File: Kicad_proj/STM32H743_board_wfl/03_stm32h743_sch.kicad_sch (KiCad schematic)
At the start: 35 parts, among them J1 GPS, J2 ESC, J3 UART, J4 Tag_Connect_6pin, U3 STM32H743VITx, U4 W25Q512JVEIQ, Y1 TSX-3225_16.0000MF18X-AC0

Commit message: update stm32 quartz caps + prebom
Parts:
- C23, C24: value 27pF -> 10pF
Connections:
- net GND: now also Y1.2 (G), Y1.4 (G)
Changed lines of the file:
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@@
 	(wire
 		(pts
+			(xy 181.356 89.154) (xy 184.15 89.154)
+		)
+		(stroke
+			(width 0)
+			(type default)
+		)
+	)
+	(wire
+		(pts
 			(xy 231.394 42.164) (xy 228.854 42.164)
 		)
@@
 			)
 		)
-		(property "Value" "27pF"
+		(property "Value" "10pF"
 			(at 156.464 99.0599 0)
 			(show_name no)
@@
 			)
 		)
-		(property "Datasheet" "https://www.mouser.pl/pl/ProductDetail/KYOCERA-AVX/04023U270JAT2A?qs=%252BdQmOuGyFcGHQXol69SFgA%3D%3D"
+		(property "Datasheet" "https://www.tme.eu/pl/details/grm1555c1h100ga01d/kondensatory-mlcc-smd/murata/"
 			(at 160.528 97.79 0)
 			(hide yes)
@@
 	)
 	(symbol
+		(lib_id "power:GND")
+		(at 184.15 89.154 90)
+		(mirror x)
+		(unit 1)
+		(body_style 1)
+		(exclude_from_sim no)
+		(in_bom yes)
+		(on_board yes)
+		(in_pos_files yes)
+		(dnp no)
+		(fields_autoplaced yes)
+		(property "Reference" "#PWR068"
+			(at 190.5 89.154 0)
+			(hide yes)
+			(show_name no)
+			(do_not_autoplace no)
+			(effects
+				(font
+					(size 1.27 1.27)
+				)
+			)
+		)
+		(property "Value" "GND"
+			(at 188.468 89.1539 90)
+			(show_name no)
+			(do_not_autoplace no)
+			(effects
+				(font
+					(size 1.27 1.27)
+				)
+				(justify right)
+			)
+		)
+		(property "Footprint" ""
+			(at 184.15 89.154 0)
+			(hide yes)
+			(show_name no)
+			(do_not_autoplace no)
+			(effects
+				(font
+					(size 1.27 1.27)
+				)
+			)
+		)
+		(property "Datasheet" ""
+			(at 184.15 89.154 0)
+			(hide yes)
+			(show_name no)
+			(do_not_autoplace no)
+			(effects
+				(font
+					(size 1.27 1.27)
+				)
+			)
+		)
+		(property "Description" "Power symbol creates a global label with name \"GND\" , ground"
+			(at 184.15 89.154 0)
+			(hide yes)
+			(show_name no)
+			(do_not_autoplace no)
+			(effects
+				(font
+					(size 1.27 1.27)
+				)
+			)
+		)
+		(pin "1"
+		)
+		(instances
+			(project "STM32H743_board_wfl"
+				(path "/3ffbaf01-8fe7-4f96-b685-21b9df9d548a/d99da23c-42db-4338-87a0-b38c4540e099"
+					(reference "#PWR068")
+					(unit 1)
+				)
+			)
+		)
+	)
+	(symbol
 		(lib_id "power:+3V3")
 		(at 316.738 117.856 0)
@@
 			)
 		)
-		(property "Value" "27pF"
+		(property "Value" "10pF"
 			(at 171.45 99.0599 0)
 			(show_name no)
@@
 			)
 		)
-		(property "Datasheet" "https://www.mouser.pl/pl/ProductDetail/KYOCERA-AVX/04023U270JAT2A?qs=%252BdQmOuGyFcGHQXol69SFgA%3D%3D"
+		(property "Datasheet" "https://www.tme.eu/pl/details/grm1555c1h100ga01d/kondensatory-mlcc-smd/murata/"
 			(at 168.148 97.79 0)
 			(hide yes)

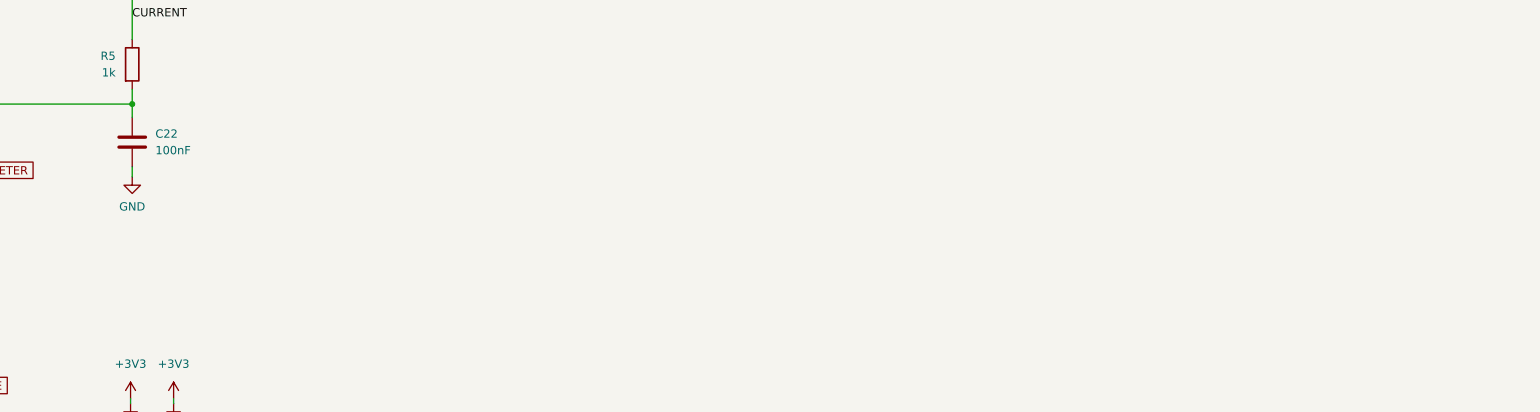
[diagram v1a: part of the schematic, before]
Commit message: LT8609 footprint cuts
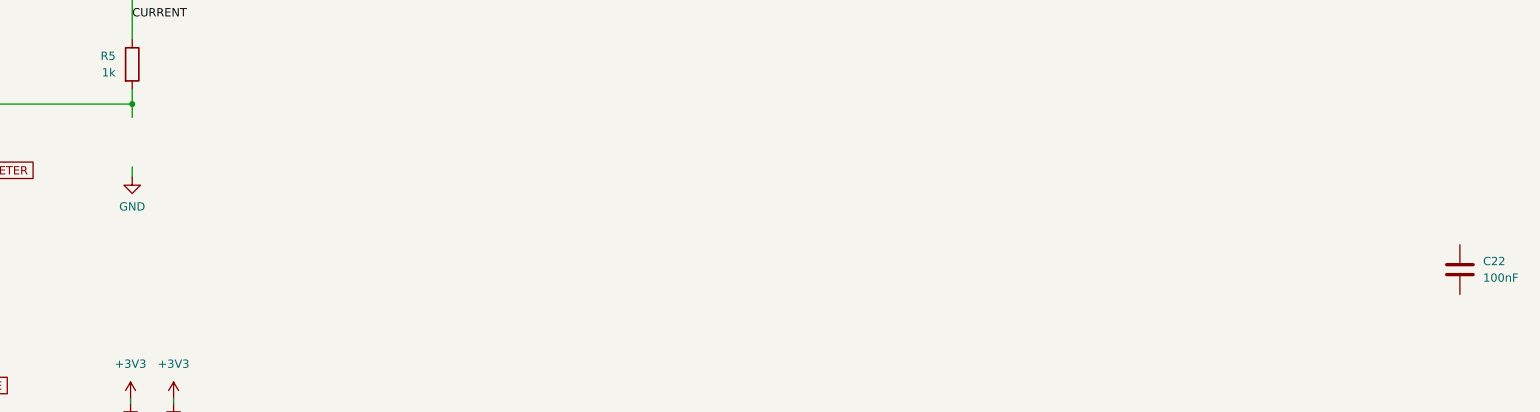
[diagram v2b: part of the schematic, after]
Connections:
- net GND: no longer C22.2
- net at R5.2, U3.22 (PA0): no longer C22.1
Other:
- moved on the sheet: C22
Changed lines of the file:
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@@
 	(symbol
 		(lib_id "Device:C")
-		(at 316.992 78.486 0)
+		(at 520.7 98.044 0)
 		(unit 1)
 		(body_style 1)
@@
 		(fields_autoplaced yes)
 		(property "Reference" "C22"
-			(at 320.548 77.2159 0)
+			(at 524.256 96.7739 0)
 			(show_name no)
 			(do_not_autoplace no)
@@
 		)
 		(property "Value" "100nF"
-			(at 320.548 79.7559 0)
+			(at 524.256 99.3139 0)
 			(show_name no)
 			(do_not_autoplace no)
@@
 		)
 		(property "Footprint" "Capacitor_SMD:C_0402_1005Metric"
-			(at 317.9572 82.296 0)
+			(at 521.6652 101.854 0)
 			(hide yes)
 			(show_name no)
@@
 		)
 		(property "Datasheet" "https://www.mouser.pl/pl/ProductDetail/TAIYO-YUDEN/MSAST105SB7104MFNB25?qs=sGAEpiMZZMs7ZEmUmaUL09vzuHXozE3EkFe3RaEcrjM8N4qw%2FjFtLg%3D%3D"
-			(at 316.992 78.486 0)
+			(at 520.7 98.044 0)
 			(hide yes)
 			(show_name no)
@@
 		)
 		(property "Description" "Unpolarized capacitor"
-			(at 316.992 78.486 0)
+			(at 520.7 98.044 0)
 			(hide yes)
 			(show_name no)

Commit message: PCB v0.7 routing part3
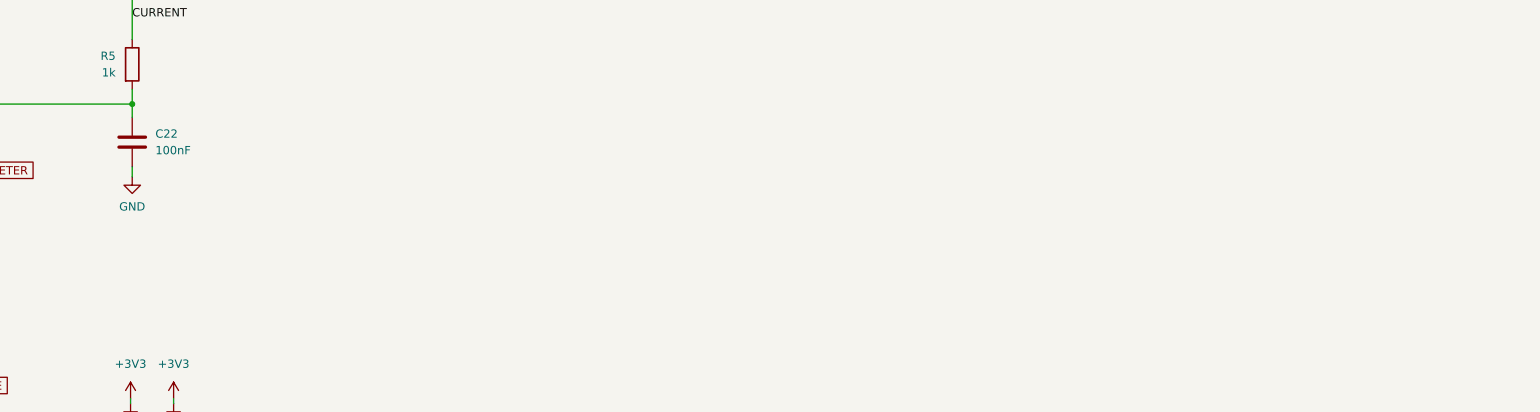
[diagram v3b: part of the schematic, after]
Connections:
- net GND: now also C22.2
- net at R5.2, U3.22 (PA0): now also C22.1
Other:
- moved on the sheet: C22
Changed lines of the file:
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@@
 	(symbol
 		(lib_id "Device:C")
-		(at 520.7 98.044 0)
+		(at 316.992 78.486 0)
 		(unit 1)
 		(body_style 1)
@@
 		(fields_autoplaced yes)
 		(property "Reference" "C22"
-			(at 524.256 96.7739 0)
+			(at 320.548 77.2159 0)
 			(show_name no)
 			(do_not_autoplace no)
@@
 		)
 		(property "Value" "100nF"
-			(at 524.256 99.3139 0)
+			(at 320.548 79.7559 0)
 			(show_name no)
 			(do_not_autoplace no)
@@
 		)
 		(property "Footprint" "Capacitor_SMD:C_0402_1005Metric"
-			(at 521.6652 101.854 0)
+			(at 317.9572 82.296 0)
 			(hide yes)
 			(show_name no)
@@
 		)
 		(property "Datasheet" "https://www.mouser.pl/pl/ProductDetail/TAIYO-YUDEN/MSAST105SB7104MFNB25?qs=sGAEpiMZZMs7ZEmUmaUL09vzuHXozE3EkFe3RaEcrjM8N4qw%2FjFtLg%3D%3D"
-			(at 520.7 98.044 0)
+			(at 316.992 78.486 0)
 			(hide yes)
 			(show_name no)
@@
 		)
 		(property "Description" "Unpolarized capacitor"
-			(at 520.7 98.044 0)
+			(at 316.992 78.486 0)
 			(hide yes)
 			(show_name no)

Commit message: PCB v1.0
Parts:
- added J5: USB, Connector_JST:JST_GH_SM04B-GHS-TB_1x04-1MP_P1.25mm_Horizontal, symbol Connector_Generic:Conn_01x04
- added Q1, Q2: AOD423, wfl_lib:TO-252-2_AOD423, symbol WFL_SYMBOL_LIB_KICAD:AOD423
- added R79, R80: 100k, Resistor_SMD:R_0603_1608Metric_Pad0.98x0.95mm_HandSolder, symbol Device:R
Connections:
- net +5V: now also Q2.3 (S)
- net +BATT: now also Q1.2 (D); no longer J2.1 (Pin_1)
- net GND: now also J5.4 (Pin_4), R79.1, R80.1
- new net: Q2.1 (G), R80.2
- new net: Q1.1 (G), R79.2
- new net USB_5V_OUT: J5.1 (Pin_1), Q2.2 (D)
- new net USB_N: J5.3 (Pin_3)
- new net USB_P: J5.2 (Pin_2)
- new net batt_safe: J2.1 (Pin_1), Q1.3 (S)
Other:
- moved on the sheet: C27, C28, J1, J2, J3, J4, R13, U4
